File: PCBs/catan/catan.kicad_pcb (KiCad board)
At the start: 2 copper layers, 95.3 x 110 mm, 65 parts, among them J1 Conn_01x04_Female, J2 Conn_01x06_Male, SW1 SW_MEC_5E, SW10 SW_MEC_5E, SW11 SW_MEC_5E, SW2 SW_MEC_5E, SW3 SW_MEC_5E, SW4 SW_MEC_5E, SW5 SW_MEC_5E, SW6 SW_MEC_5E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

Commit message: wire registers together
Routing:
- net Net-(U2-Pad24): track 0.00 -> 23.6 mm, vias 0 -> 1
- net Net-(U2-Pad23): track 0.00 -> 22.3 mm
- net Net-(U5-Pad9): track 0.00 -> 9.19 mm

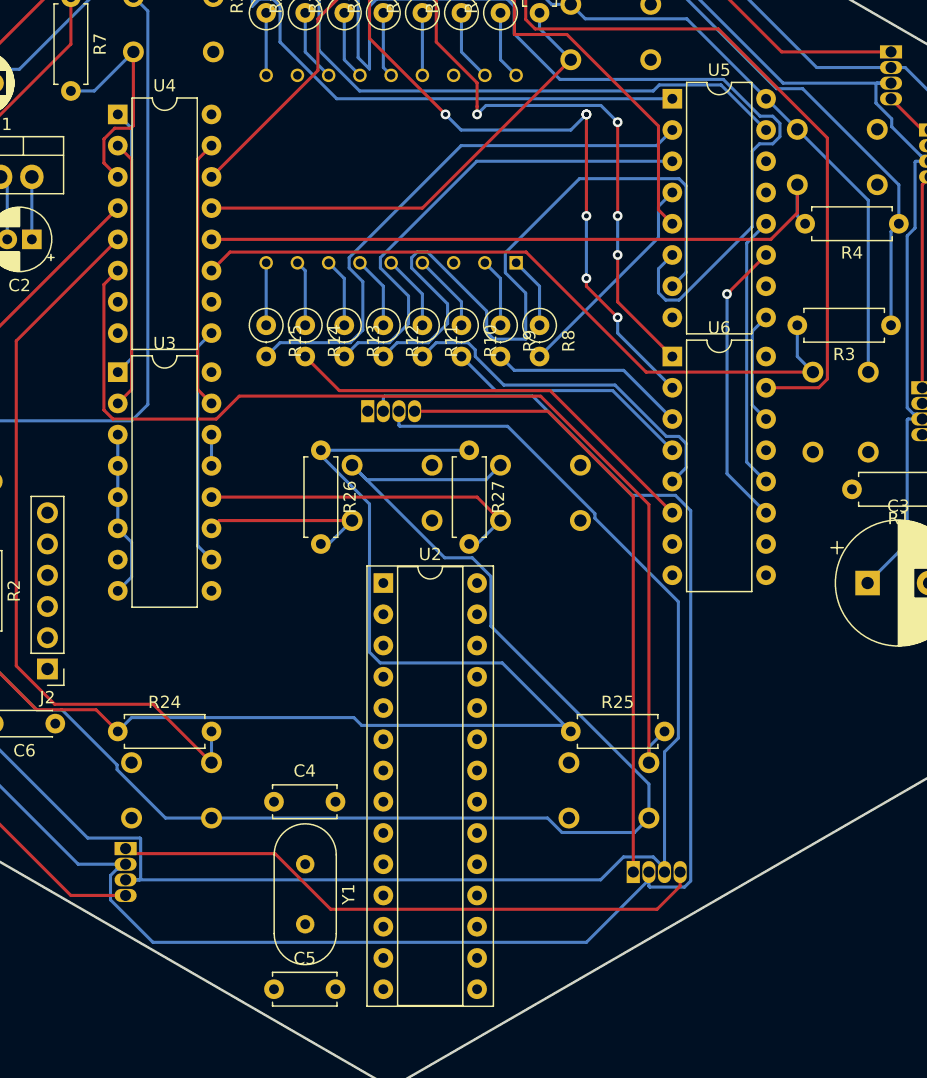
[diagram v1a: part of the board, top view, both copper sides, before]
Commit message: wire sub-components to arduino
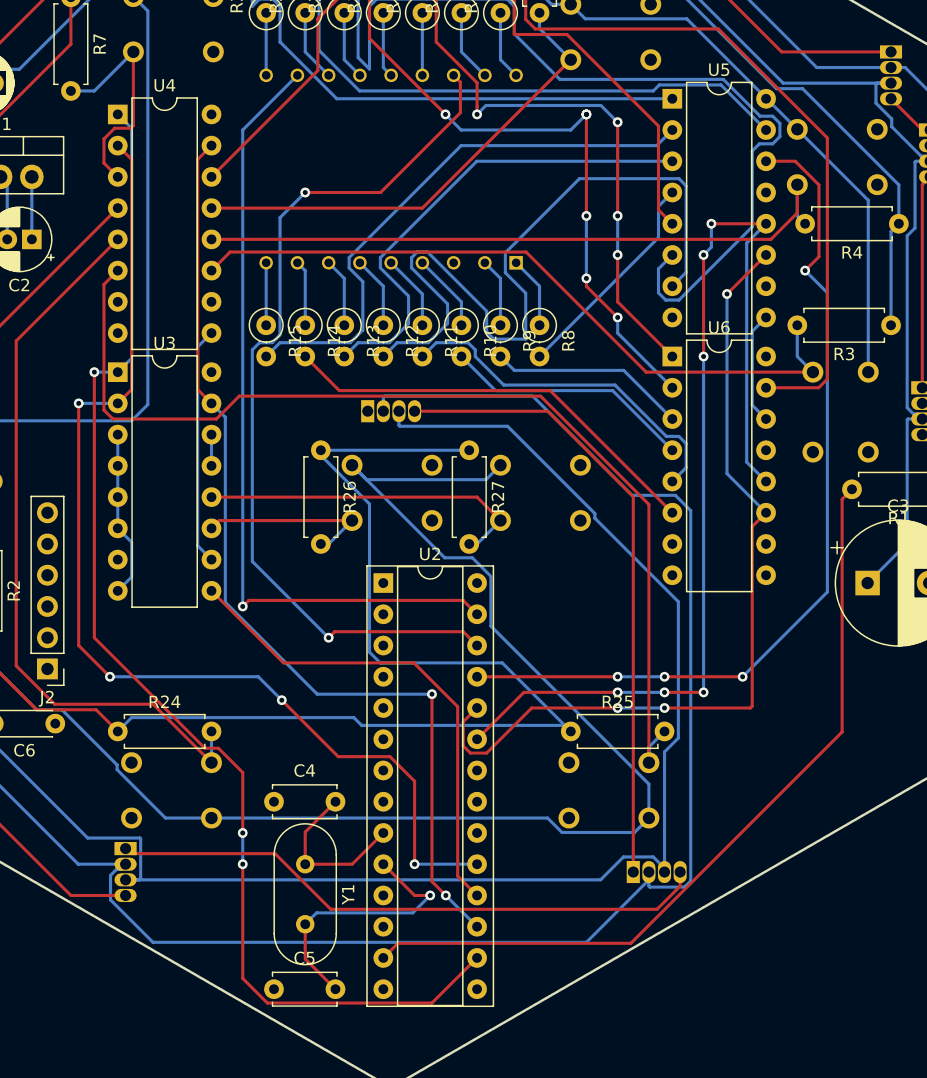
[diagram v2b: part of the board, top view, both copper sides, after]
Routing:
- net Net-(U2-Pad16): track 21.9 -> 100.1 mm, vias 0 -> 3
- net Net-(DS1-Pad16): track 0.00 -> 72.5 mm, vias 0 -> 2
- net Net-(U2-Pad25): track 0.00 -> 70.7 mm, vias 0 -> 4
- net Net-(U2-Pad19): track 21.9 -> 88.4 mm, vias 0 -> 4
- net Net-(R1-Pad2): track 0.00 -> 65.0 mm
- net Net-(DS1-Pad11): track 0.00 -> 64.7 mm, vias 0 -> 1
- net Net-(U2-Pad23): track 22.3 -> 85.1 mm, vias 0 -> 6
- net Net-(U2-Pad17): track 21.9 -> 78.8 mm, vias 0 -> 2
- net Net-(U2-Pad24): track 23.6 -> 68.6 mm, vias 1 -> 3
- net Net-(U2-Pad18): track 0.00 -> 39.9 mm
- net Net-(C5-Pad2): track 0.00 -> 22.3 mm, vias 0 -> 1
- net Net-(C4-Pad2): track 0.00 -> 13.5 mm

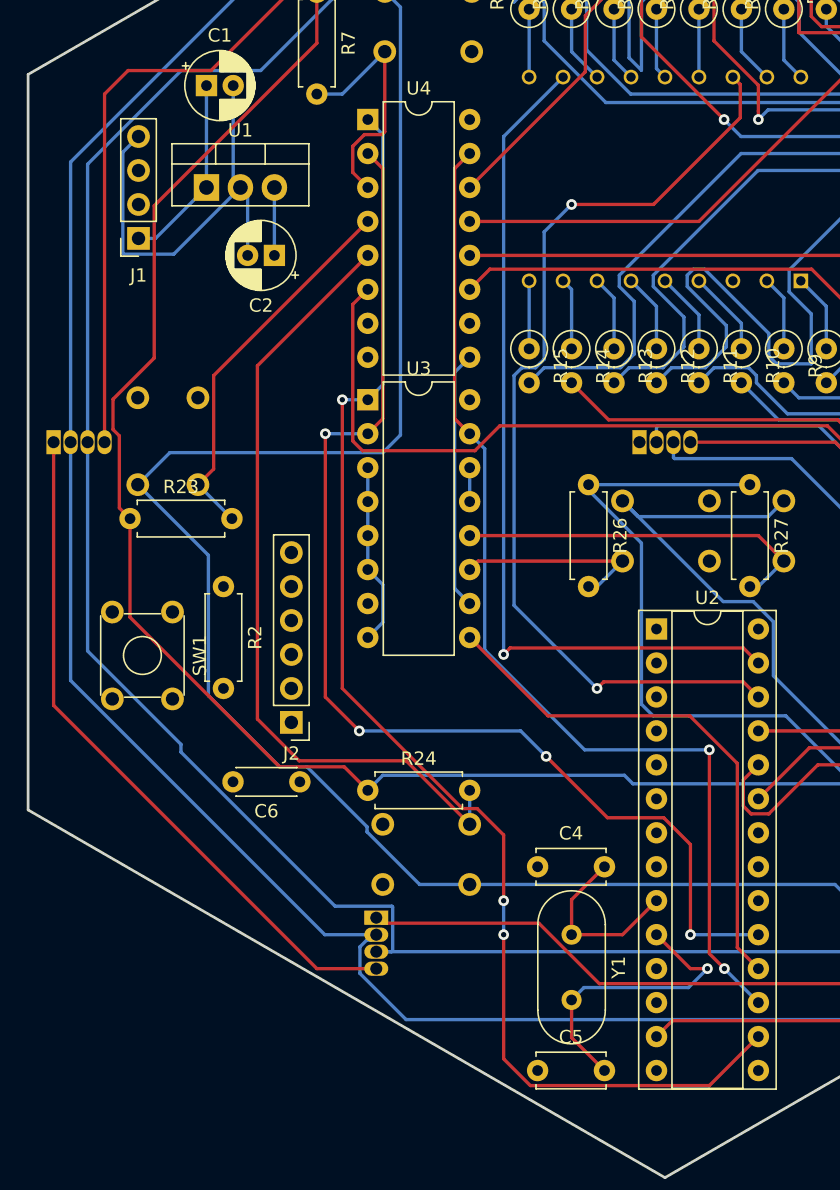
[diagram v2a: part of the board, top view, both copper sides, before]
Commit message: wire actor port
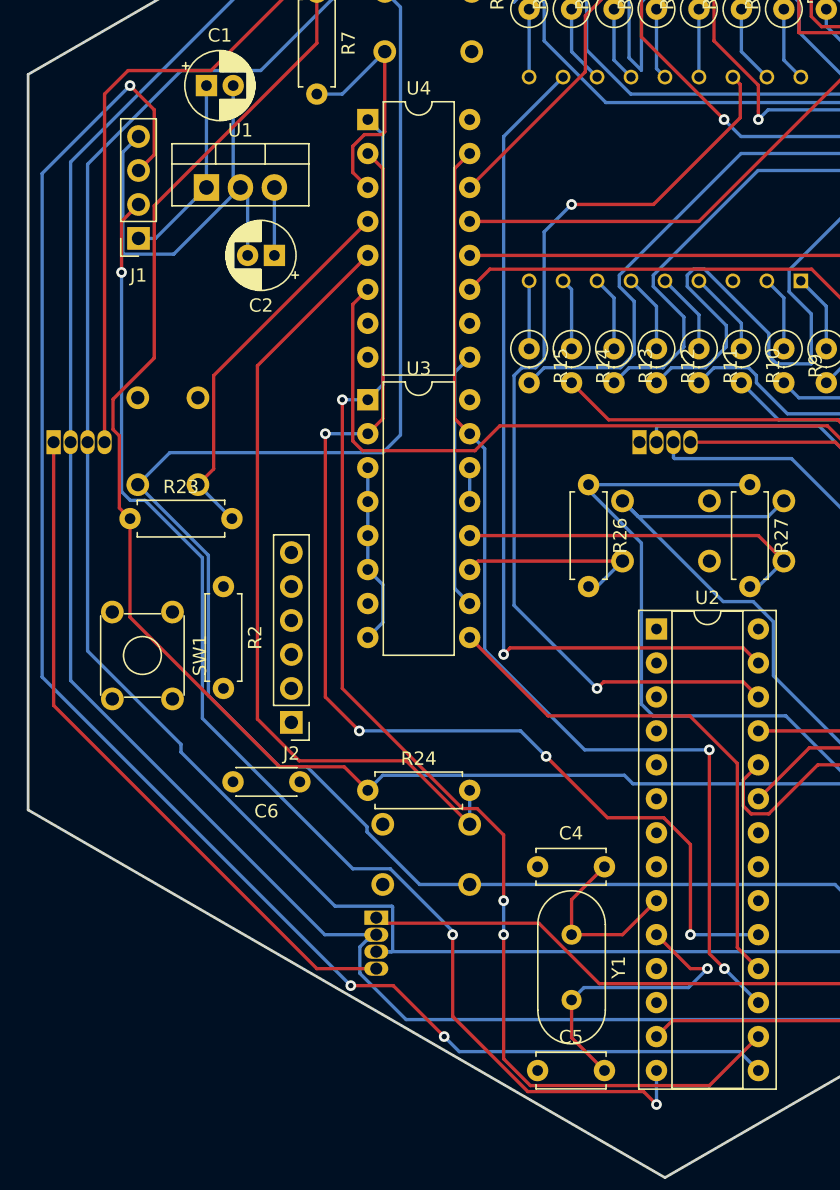
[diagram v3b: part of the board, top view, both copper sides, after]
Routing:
- net Net-(J1-Pad3): track 0.00 -> 120.3 mm, vias 0 -> 3
- net Net-(J1-Pad2): track 0.00 -> 94.3 mm, vias 0 -> 3
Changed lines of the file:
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@@
     (thickness 1.6)
     (drawings 12)
-    (tracks 674)
+    (tracks 713)
     (zones 0)
     (modules 65)
@@
   (segment (start 137.16 80.01) (end 135.255 78.105) (width 0.25) (layer B.Cu) (net 35))
   (segment (start 137.16 83.185) (end 137.16 80.01) (width 0.25) (layer B.Cu) (net 35))
+  (segment (start 86.900001 68.674999) (end 86.900001 65.310001) (width 0.25) (layer F.Cu) (net 36))
+  (segment (start 85.725 69.85) (end 86.900001 68.674999) (width 0.25) (layer F.Cu) (net 36))
+  (segment (start 86.900001 65.310001) (end 85.09 63.5) (width 0.25) (layer F.Cu) (net 36))
+  (segment (start 85.09 63.5) (end 85.09 63.5) (width 0.25) (layer F.Cu) (net 36))
+  (via (at 85.09 63.5) (size 0.8) (drill 0.4) (layers F.Cu B.Cu) (net 36))
+  (segment (start 78.514999 70.075001) (end 78.514999 107.724999) (width 0.25) (layer B.Cu) (net 36))
+  (segment (start 85.09 63.5) (end 78.514999 70.075001) (width 0.25) (layer B.Cu) (net 36))
+  (segment (start 78.514999 107.724999) (end 101.6 130.81) (width 0.25) (layer B.Cu) (net 36))
+  (segment (start 101.6 130.81) (end 101.6 130.81) (width 0.25) (layer B.Cu) (net 36))
+  (via (at 101.6 130.81) (size 0.8) (drill 0.4) (layers F.Cu B.Cu) (net 36))
+  (segment (start 101.6 130.81) (end 104.775 130.81) (width 0.25) (layer F.Cu) (net 36))
+  (segment (start 104.775 130.81) (end 108.585 134.62) (width 0.25) (layer F.Cu) (net 36))
+  (segment (start 108.585 134.62) (end 108.585 134.62) (width 0.25) (layer F.Cu) (net 36))
+  (via (at 108.585 134.62) (size 0.8) (drill 0.4) (layers F.Cu B.Cu) (net 36))
+  (segment (start 130.665001 135.745001) (end 132.08 137.16) (width 0.25) (layer B.Cu) (net 36))
+  (segment (start 109.710001 135.745001) (end 130.665001 135.745001) (width 0.25) (layer B.Cu) (net 36))
+  (segment (start 108.585 134.62) (end 109.710001 135.745001) (width 0.25) (layer B.Cu) (net 36))
+  (segment (start 85.725 72.39) (end 84.455 73.66) (width 0.25) (layer F.Cu) (net 37))
+  (segment (start 84.455 73.66) (end 84.455 77.47) (width 0.25) (layer F.Cu) (net 37))
+  (segment (start 84.455 77.47) (end 84.455 77.47) (width 0.25) (layer F.Cu) (net 37))
+  (via (at 84.455 77.47) (size 0.8) (drill 0.4) (layers F.Cu B.Cu) (net 37))
+  (segment (start 101.749999 122.069999) (end 104.554001 122.069999) (width 0.25) (layer B.Cu) (net 37))
+  (segment (start 90.499989 110.819989) (end 101.749999 122.069999) (width 0.25) (layer B.Cu) (net 37))
+  (segment (start 90.499989 98.811399) (end 90.499989 110.819989) (width 0.25) (layer B.Cu) (net 37))
+  (segment (start 104.554001 122.069999) (end 109.22 126.735998) (width 0.25) (layer B.Cu) (net 37))
+  (segment (start 86.208591 94.520001) (end 90.499989 98.811399) (width 0.25) (layer B.Cu) (net 37))
+  (segment (start 85.105999 94.520001) (end 86.208591 94.520001) (width 0.25) (layer B.Cu) (net 37))
+  (segment (start 84.455 93.869002) (end 85.105999 94.520001) (width 0.25) (layer B.Cu) (net 37))
+  (segment (start 84.455 77.47) (end 84.455 93.869002) (width 0.25) (layer B.Cu) (net 37))
+  (segment (start 109.22 126.735998) (end 109.22 127) (width 0.25) (layer B.Cu) (net 37))
+  (segment (start 109.22 127) (end 109.22 127) (width 0.25) (layer B.Cu) (net 37))
+  (via (at 109.22 127) (size 0.8) (drill 0.4) (layers F.Cu B.Cu) (net 37))
+  (segment (start 114.843599 138.735011) (end 123.495011 138.735011) (width 0.25) (layer F.Cu) (net 37))
+  (segment (start 109.22 133.111412) (end 114.843599 138.735011) (width 0.25) (layer F.Cu) (net 37))
+  (segment (start 109.22 127) (end 109.22 133.111412) (width 0.25) (layer F.Cu) (net 37))
+  (segment (start 123.495011 138.735011) (end 124.46 139.7) (width 0.25) (layer F.Cu) (net 37))
+  (segment (start 124.46 139.7) (end 124.46 139.7) (width 0.25) (layer F.Cu) (net 37))
+  (via (at 124.46 139.7) (size 0.8) (drill 0.4) (layers F.Cu B.Cu) (net 37))
+  (segment (start 124.46 139.7) (end 124.46 137.16) (width 0.25) (layer B.Cu) (net 37))
   (segment (start 125.651025 133.428975) (end 124.46 134.62) (width 0.25) (layer F.Cu) (net 40))
   (segment (start 144.582435 133.428975) (end 125.651025 133.428975) (width 0.25) (layer F.Cu) (net 40))

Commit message: done with pcb?
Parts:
- added REF**: MountingHole_2.7mm_M2.5, MountingHole:MountingHole_2.7mm_M2.5, F.Cu at (81.8, 115.2)
- added REF**: MountingHole_2.7mm_M2.5, MountingHole:MountingHole_2.7mm_M2.5, F.Cu at (132.1, 46.4)
- added REF**: MountingHole_2.7mm_M2.5, MountingHole:MountingHole_2.7mm_M2.5, F.Cu at (168.4, 115.2)
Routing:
- net GND: track 649.8 -> 996.8 mm, vias 0 -> 6
- net Net-(C2-Pad1): track 611.8 -> 956.8 mm, vias 0 -> 6
- net Net-(C6-Pad2): track 0.00 -> 56.5 mm, vias 0 -> 1
- net Net-(J2-Pad2): track 0.00 -> 46.4 mm, vias 0 -> 5
- net Net-(J2-Pad3): track 0.00 -> 38.1 mm, vias 0 -> 4
- net Net-(C6-Pad1): track 0.00 -> 9.20 mm, vias 0 -> 1

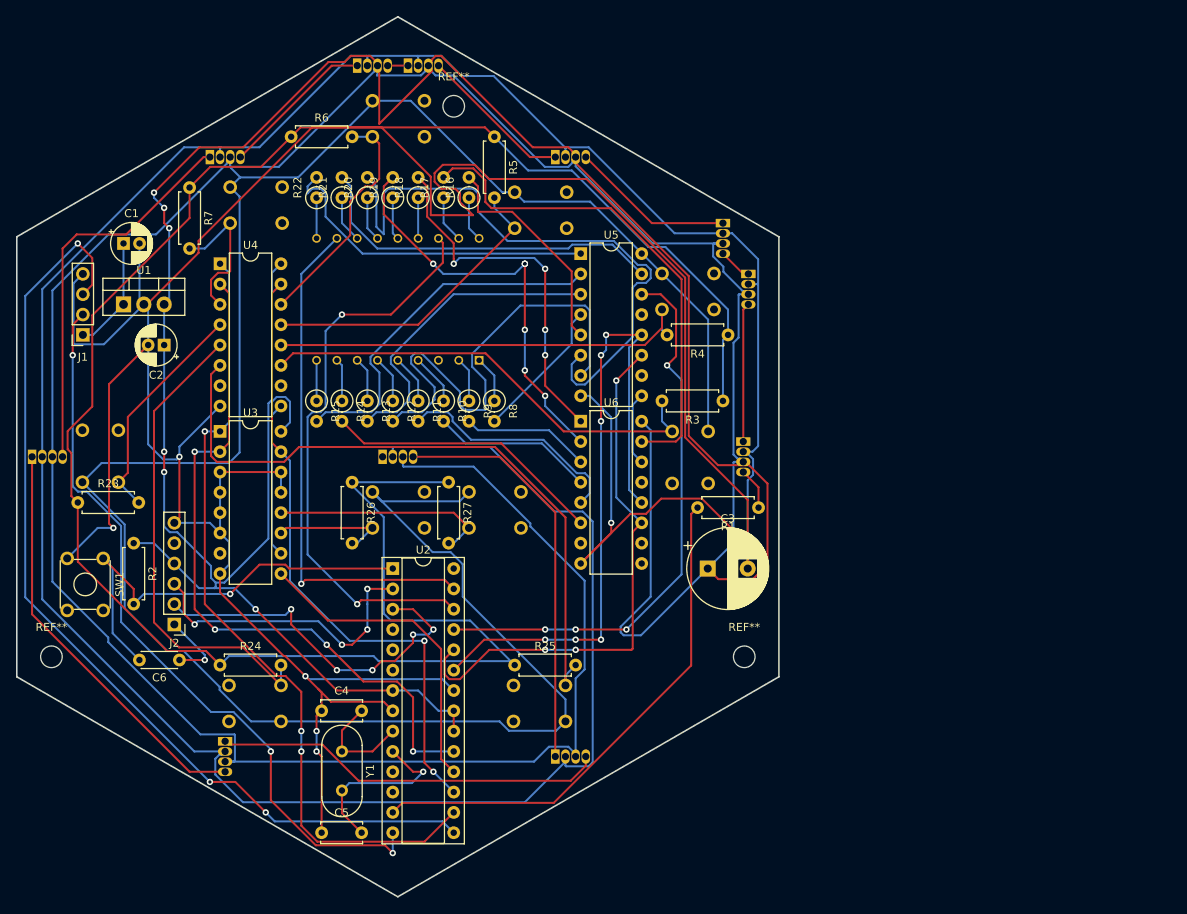
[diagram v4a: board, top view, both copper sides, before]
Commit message: updating to 16 segment
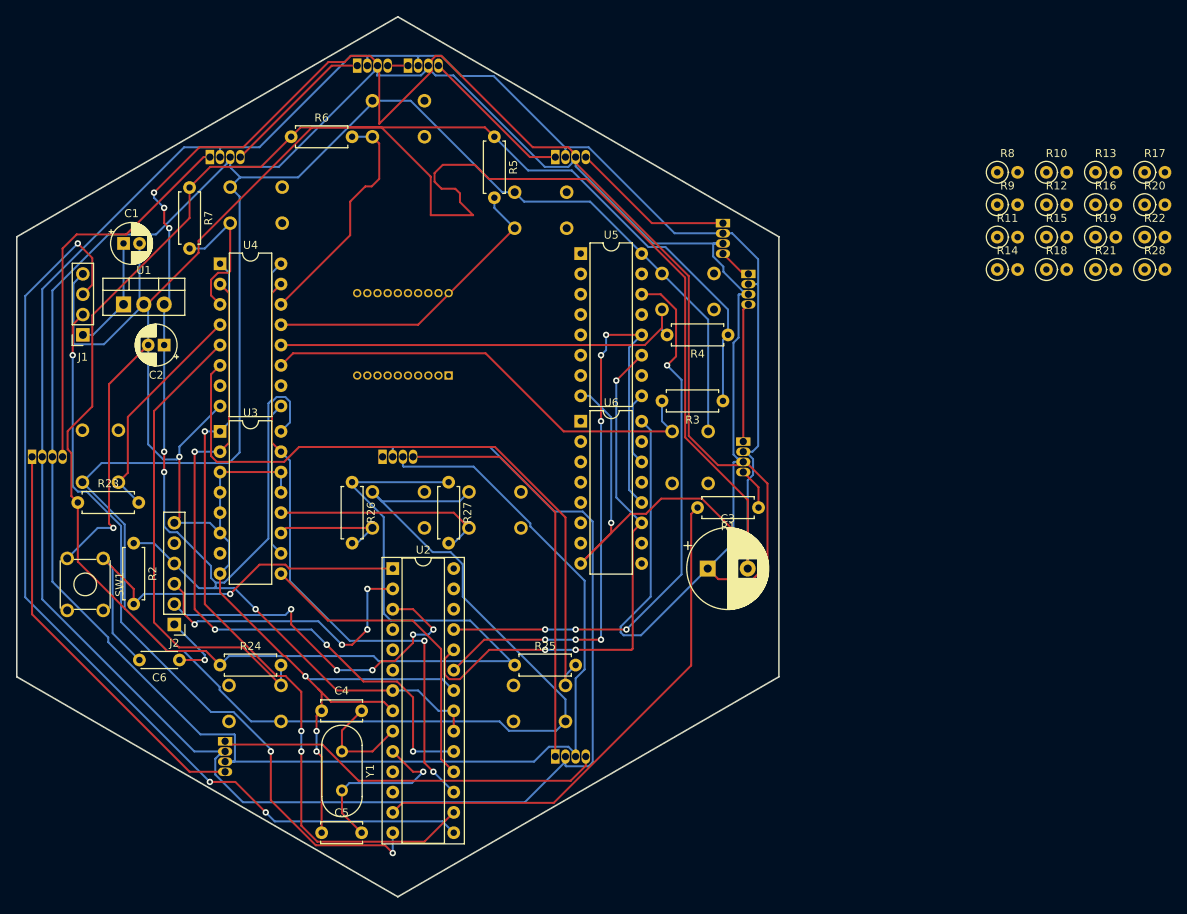
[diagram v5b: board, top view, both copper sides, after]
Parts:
- removed REF** (x3): MountingHole_2.7mm_M2.5, MountingHole:MountingHole_2.7mm_M2.5
- added R28: R, Resistor_THT:R_Axial_DIN0207_L6.3mm_D2.5mm_P2.54mm_Vertical, F.Cu at (218.4, 66.8)
- DS1: value HDSP-A22C -> LTP-3862G; footprint SamacSys_Parts:DIPS1524W51P254L2520H725Q18N -> SamacSys_Parts:DIPS1030W45P127L1690H645Q20N
- moved R22 103.6 mm to (218.4, 62.7), turned to 0 degrees
- moved R20 97.2 mm to (218.4, 58.7), turned to 0 degrees
- moved R13 95.4 mm to (212.3, 54.6), turned to 0 degrees
- moved R21 94.6 mm to (212.3, 66.8), turned to 0 degrees
- moved R15 93.5 mm to (206.2, 62.7), turned to 0 degrees
- moved R19 88.0 mm to (212.3, 62.7), turned to 0 degrees
- moved R17 87.7 mm to (218.4, 54.6), turned to 0 degrees
- moved R12 85.3 mm to (206.2, 58.7), turned to 0 degrees
- moved R14 83.5 mm to (200.0, 66.8), turned to 0 degrees
- moved R10 80.6 mm to (206.2, 54.6), turned to 0 degrees
- moved R18 79.0 mm to (206.2, 66.8), turned to 0 degrees
- moved R16 78.3 mm to (212.3, 58.7), turned to 0 degrees
- moved R11 75.2 mm to (200.0, 62.7), turned to 0 degrees
- moved R9 70.4 mm to (200.0, 58.7), turned to 0 degrees
- moved R8 69.1 mm to (200.0, 54.6), turned to 0 degrees
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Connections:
- DS1 pad 1: Net-(DS1-Pad1) -> (no net)
- DS1 pad 11: Net-(DS1-Pad11) -> (no net)
- DS1 pad 12: Net-(DS1-Pad12) -> (no net)
- DS1 pad 13: Net-(DS1-Pad13) -> (no net)
- DS1 pad 14: Net-(DS1-Pad14) -> (no net)
- DS1 pad 15: Net-(DS1-Pad15) -> (no net)
- DS1 pad 16: Net-(DS1-Pad16) -> (no net)
- DS1 pad 17: Net-(DS1-Pad17) -> (no net)
- DS1 pad 18: Net-(DS1-Pad18) -> (no net)
- DS1 pad 2: Net-(DS1-Pad2) -> (no net)
- DS1 pad 5: Net-(DS1-Pad5) -> (no net)
- DS1 pad 6: Net-(DS1-Pad6) -> (no net)
- DS1 pad 7: Net-(DS1-Pad7) -> (no net)
- DS1 pad 8: Net-(DS1-Pad8) -> (no net)
- DS1 pad 9: Net-(DS1-Pad9) -> (no net)
- R10 pad 1: Net-(DS1-Pad4) -> (no net)
- R11 pad 1: Net-(DS1-Pad5) -> (no net)
- R12 pad 1: Net-(DS1-Pad6) -> (no net)
- R13 pad 1: Net-(DS1-Pad7) -> (no net)
- R14 pad 1: Net-(DS1-Pad8) -> (no net)
- R15 pad 1: Net-(DS1-Pad9) -> (no net)
- R16 pad 1: Net-(DS1-Pad18) -> (no net)
- R17 pad 1: Net-(DS1-Pad17) -> (no net)
- R18 pad 1: Net-(DS1-Pad15) -> (no net)
- R19 pad 1: Net-(DS1-Pad14) -> (no net)
- R20 pad 1: Net-(DS1-Pad13) -> (no net)
- R21 pad 1: Net-(DS1-Pad12) -> (no net)
- R22 pad 1: Net-(DS1-Pad10) -> (no net)
- R8 pad 1: Net-(DS1-Pad1) -> (no net)
- R9 pad 1: Net-(DS1-Pad2) -> (no net)
- U2 pad 26: Net-(DS1-Pad16) -> Net-(DS1-Pad4)
- U2 pad 27: Net-(DS1-Pad11) -> Net-(DS1-Pad10)
- U5 pad 1: Net-(R22-Pad2) -> Net-(R9-Pad2)
- U5 pad 15: Net-(R21-Pad2) -> Net-(R8-Pad2)
- U5 pad 2: Net-(R15-Pad2) -> Net-(R10-Pad2)
- U5 pad 3: Net-(R13-Pad2) -> Net-(R11-Pad2)
- U5 pad 4: Net-(R8-Pad2) -> Net-(R12-Pad2)
- U5 pad 5: Net-(R16-Pad2) -> Net-(R13-Pad2)
- U5 pad 6: Net-(R20-Pad2) -> Net-(R14-Pad2)
- U5 pad 7: Net-(R12-Pad2) -> Net-(R15-Pad2)
- U6 pad 1: Net-(R18-Pad2) -> Net-(R17-Pad2)
- U6 pad 15: Net-(R17-Pad2) -> Net-(R16-Pad2)
- U6 pad 2: Net-(R19-Pad2) -> Net-(R18-Pad2)
- U6 pad 3: Net-(R9-Pad2) -> Net-(R19-Pad2)
- U6 pad 4: Net-(R10-Pad2) -> Net-(R20-Pad2)
- U6 pad 5: Net-(R11-Pad2) -> Net-(R21-Pad2)
- U6 pad 6: Net-(R14-Pad2) -> Net-(R22-Pad2)
- U6 pad 7: (no net) -> Net-(R28-Pad2)
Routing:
- net Net-(R20-Pad2): track 76.0 -> 0.00 mm
- net Net-(DS1-Pad16): track 72.5 -> 0.00 mm, vias 2 -> 0
- net Net-(DS1-Pad11): track 64.7 -> 0.00 mm, vias 1 -> 0
- net Net-(R17-Pad2): track 62.4 -> 0.00 mm
- net Net-(R12-Pad2): track 60.1 -> 0.00 mm
- net Net-(R19-Pad2): track 51.4 -> 0.00 mm, vias 6 -> 0
- net Net-(R18-Pad2): track 45.8 -> 0.00 mm, vias 4 -> 0
- net Net-(R15-Pad2): track 45.7 -> 0.00 mm
- net Net-(R21-Pad2): track 45.5 -> 0.00 mm
- net Net-(R22-Pad2): track 41.9 -> 0.00 mm
- net Net-(R13-Pad2): track 39.6 -> 0.00 mm
- net Net-(R14-Pad2): track 35.1 -> 0.00 mm
- net Net-(R11-Pad2): track 29.2 -> 0.00 mm
- net Net-(R16-Pad2): track 28.0 -> 0.00 mm
- net Net-(R10-Pad2): track 20.3 -> 0.00 mm
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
